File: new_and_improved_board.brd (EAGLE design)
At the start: 48.2 x 56.8 mm, 23 parts, among them J4 455-1750-1-ND, Q2 IRF3704L-V

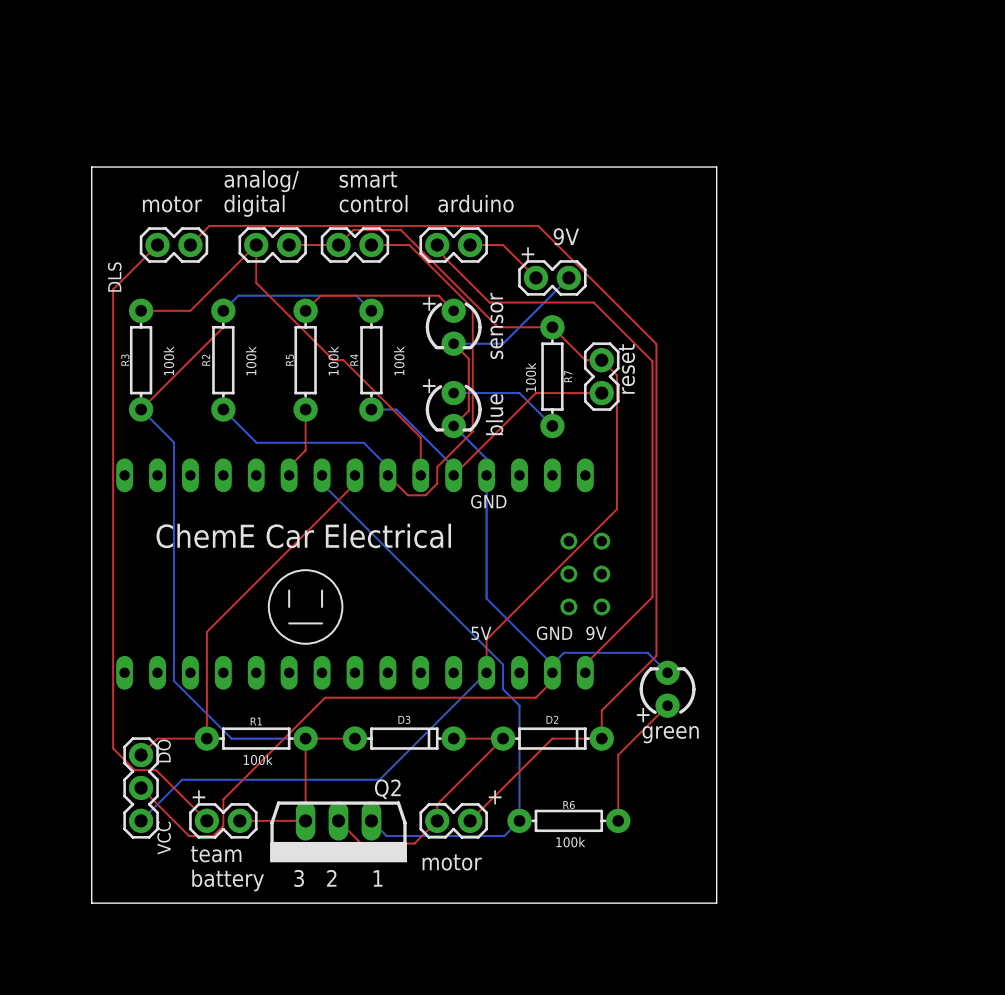
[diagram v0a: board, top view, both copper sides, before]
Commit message: added ground and power planes, and changed resistor values/added resistor after the mosfet gate
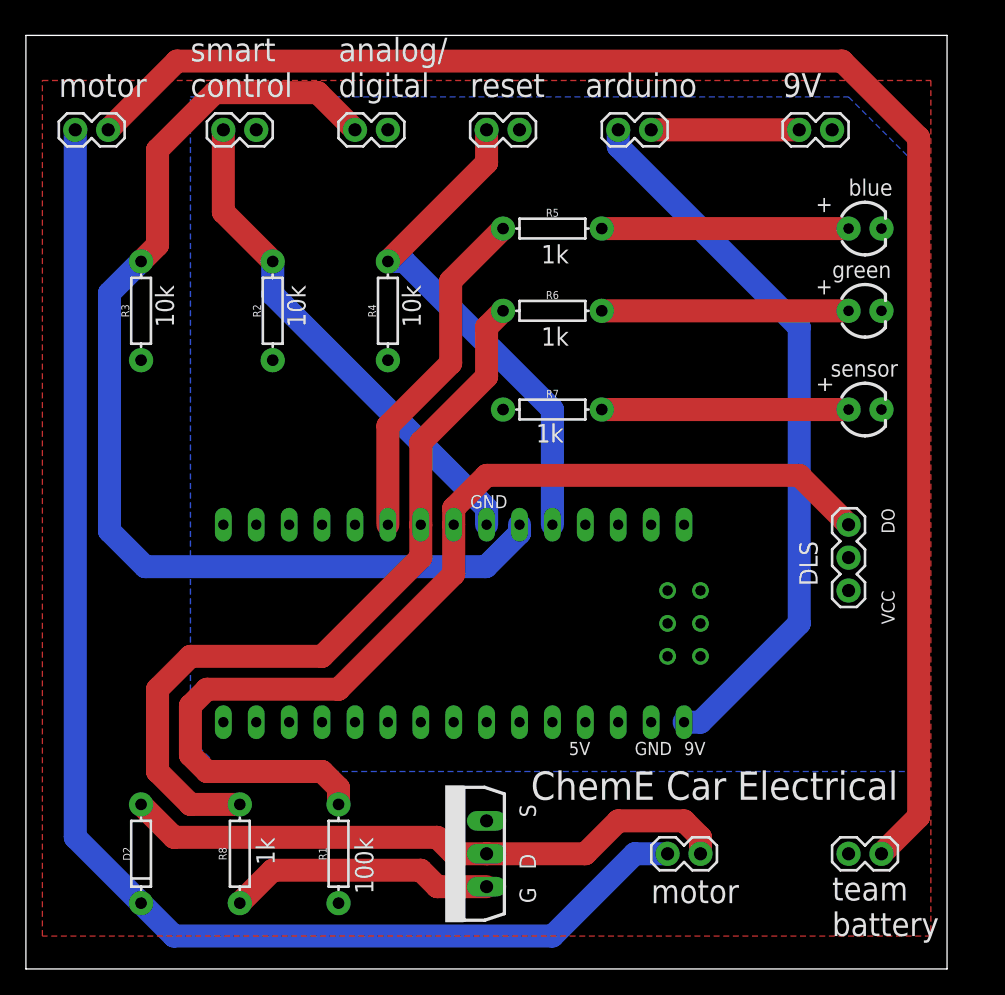
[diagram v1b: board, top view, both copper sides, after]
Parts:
- removed D3: 200mA/100V/1V, SparkFun-DiscreteSemi:DIODE-1N4148
- added R8: 1M, SparkFun-Resistors:AXIAL-0.3
- moved J4 57.4 mm to (58.4, 29.2)
- moved J3 52.1 mm to (61.0, 3.81), turned to 180 degrees
- moved R6 39.4 mm to (35.6, 45.7)
- moved D2 33.0 mm to (3.81, 3.81), turned to 270 degrees
- moved D5 32.9 mm to (59.7, 45.7), turned to 0 degrees
- moved D4 32.7 mm to (59.7, 52.1), turned to 0 degrees
- moved D6 31.7 mm to (59.7, 38.1), turned to 0 degrees
- moved J2 23.3 mm to (54.6, 59.7)
- moved R5 21.6 mm to (35.6, 52.1), turned to 180 degrees
- moved S5 18.9 mm to (33.0, 59.7), turned to 180 degrees
- moved S1 16.6 mm to (43.2, 59.7)
- moved J1 15.5 mm to (44.5, 3.81), turned to 0 degrees
- moved S3 12.6 mm to (-1.27, 59.7), turned to 0 degrees
- moved Q2 11.7 mm to (30.5, 3.81), turned to 90 degrees
- moved S4 11.7 mm to (22.9, 59.7)
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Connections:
- net N$12 renamed 9VBAT
- net N$13 renamed 9V
- net N$16 renamed 5V
- net GND: now also J3.2, Q2.3, R1.P$2, R2.P$2, R3.P$2, R4.P$2
- net N$1: now also R8.P$2; no longer Q2.1
- net N$2: no longer D3.C
- net N$3: now also Q2.1, R8.P$1; no longer D3.A, J3.2, Q2.3, R1.P$2, R2.P$2, R3.P$2, R4.P$2
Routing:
- net GND: track 90.5 -> 0.00 mm
- net 5V: track 89.0 -> 0.00 mm
- net N$15: track 49.8 -> 123.7 mm
- net N$3: track 71.9 -> 20.6 mm
- net N$4: track 30.7 -> 80.3 mm
- net N$6: track 34.5 -> 83.7 mm
- net N$2: track 21.3 -> 47.6 mm
- net N$8: track 5.61 -> 26.5 mm
- net N$11: track 85.4 -> 106.1 mm
- net N$7: track 22.9 -> 39.6 mm
- net N$1: track 45.4 -> 60.0 mm
- net N$17: track 8.67 -> 19.1 mm
- net 9V: track 46.7 -> 55.9 mm
- net N$10: track 10.5 -> 19.1 mm
- net N$9: track 12.4 -> 19.1 mm
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- added copper zone on layer 16, net 5V
- added copper zone on layer 1, net GND
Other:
- board size 48.2 x 56.8 mm -> 71.1 x 72.1 mm
- board text added: "10k"
- board text added: "1k"
- board text added: "D"
- board text added: "G"
- board text added: "S"
- board text removed: "1"
- board text removed: "2"
- board text removed: "3"
